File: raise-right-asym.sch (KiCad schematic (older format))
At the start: 102 parts, among them IC1 ATTINY88-A, J1 USB_C_Receptacle_16pin, P1 CONN_01X01, P2 CONN_01X01, P3 CONN_01X01, P4 CONN_01X01, P5 CONN_01X01, P6 CONN_01X01, P7 CONN_01X01, P8 CONN_02X03, Q1 Q_PMOS_GSD, SW1 SW_PUSH, SW10 SW_PUSH, SW11 SW_PUSH, SW12 SW_PUSH, SW13 SW_PUSH, SW14 SW_PUSH, SW15 SW_PUSH, SW16 SW_PUSH, SW17 SW_PUSH, SW18 SW_PUSH, SW19 SW_PUSH, SW2 SW_PUSH, SW20 SW_PUSH, SW21 SW_PUSH, SW22 SW_PUSH, SW23 SW_PUSH, SW24 SW_PUSH, SW25 SW_PUSH, SW26 SW_PUSH, SW27 SW_PUSH, SW28 SW_PUSH, SW29 SW_PUSH, SW3 SW_PUSH, SW30 SW_PUSH, SW31 SW_PUSH, SW32 SW_PUSH, SW33 SW_PUSH, SW34 SW_PUSH, SW4 SW_PUSH, SW5 SW_PUSH, SW6 SW_PUSH, SW7 SW_PUSH, SW8 SW_PUSH, SW9 SW_PUSH, U1 ss39et

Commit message: pre align
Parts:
- U1: supplier Value -> Honeywell; supplier PN Value -> SS39ET
- renumbered P5 to T1, P6 to T2, P7 to T3
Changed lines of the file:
@@
 EESchema Schematic File Version 3
 LIBS:raise-right-asym-cache
-LIBS:power
-LIBS:74xx
 EELAYER 26 0
 EELAYER END
@@
 $EndComp
 $Comp
-L CONN_01X01 P5
+L CONN_01X01 T1
 U 1 1 59D8FBB7
 P 5050 5650
-F 0 "P5" H 5128 5691 50  0000 L CNN
+F 0 "T1" H 5128 5691 50  0000 L CNN
 F 1 "CONN_01X01" H 5128 5600 50  0000 L CNN
 F 2 "raise_fp:MountingHole_5.5mm" H 5050 5650 50  0001 C CNN
@@
 D
 $Comp
-L CONN_01X01 P6
+L CONN_01X01 T2
 U 1 1 5A32AD50
 P 5050 5800
-F 0 "P6" H 5128 5841 50  0000 L CNN
+F 0 "T2" H 5128 5841 50  0000 L CNN
 F 1 "CONN_01X01" H 5128 5750 50  0000 L CNN
 F 2 "raise_fp:MountingHole_5.5mm" H 5050 5800 50  0001 C CNN
@@
 $EndComp
 $Comp
-L CONN_01X01 P7
+L CONN_01X01 T3
 U 1 1 5A32AD56
 P 5050 5950
-F 0 "P7" H 5128 5991 50  0000 L CNN
+F 0 "T3" H 5128 5991 50  0000 L CNN
 F 1 "CONN_01X01" H 5128 5900 50  0000 L CNN
 F 2 "raise_fp:MountingHole_5.5mm" H 5050 5950 50  0001 C CNN
@@
 F 3 "http://www.farnell.com/datasheets/2007294.pdf?_ga=2.106159619.1235724654.1525704504-2043240940.1516888894" H 3850 1350 60  0001 C CNN
 F 4 "2292924" H 3850 1000 60  0001 C CNN "farnell #"
-F 5 "Value" H 3850 1000 60  0001 C CNN "supplier"
-F 6 "Value" H 3850 1000 60  0001 C CNN "supplier PN"
+F 5 "Honeywell" H 3850 1000 60  0001 C CNN "supplier"
+F 6 "SS39ET" H 3850 1000 60  0001 C CNN "supplier PN"
 F 7 "Value" H 3850 1000 60  0001 C CNN "MOQ"
 F 8 "Value" H 3850 1000 60  0001 C CNN "leadtime"

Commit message: post align
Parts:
- renumbered SW-ISO-16 to SW_ISO_16, SW-ISO-8 to SW_ISO_8
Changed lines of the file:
@@
 hall
 $Comp
-L SW_PUSH SW-ISO-8
+L SW_PUSH SW_ISO_8
 U 1 1 5AE3302A
 P 5050 1950
-F 0 "SW-ISO-8" H 5050 2205 50  0000 C CNN
+F 0 "SW_ISO_8" H 5050 2205 50  0000 C CNN
 F 1 "SW_PUSH" H 5050 2114 50  0000 C CNN
 F 2 "raise_fp:kailhsocket-cherry" H 5050 1950 50  0001 C CNN
@@
 $EndComp
 $Comp
-L SW_PUSH SW-ISO-16
+L SW_PUSH SW_ISO_16
 U 1 1 5AE3364E
 P 5050 2650
-F 0 "SW-ISO-16" H 5050 2905 50  0000 C CNN
+F 0 "SW_ISO_16" H 5050 2905 50  0000 C CNN
 F 1 "SW_PUSH" H 5050 2814 50  0000 C CNN
 F 2 "raise_fp:kailhsocket-cherry" H 5050 2650 50  0001 C CNN

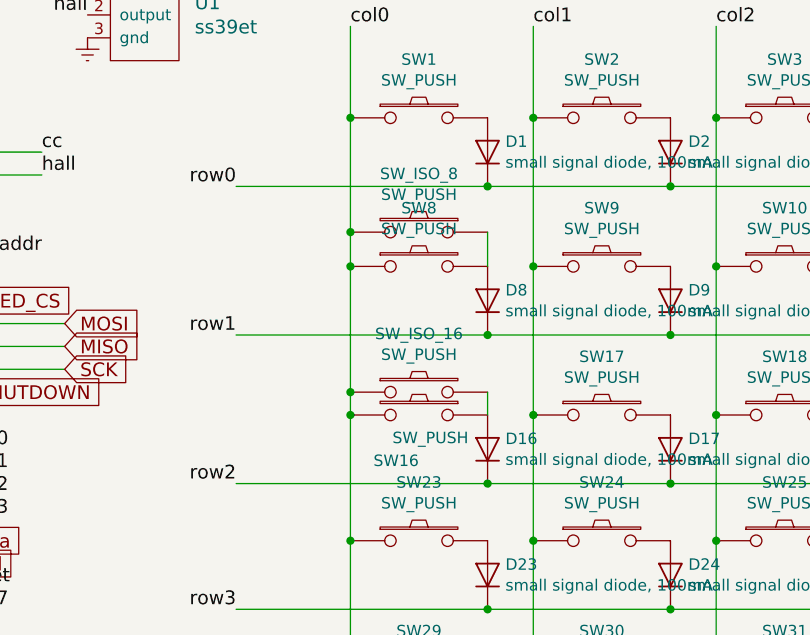
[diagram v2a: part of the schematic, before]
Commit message: fixed diodes
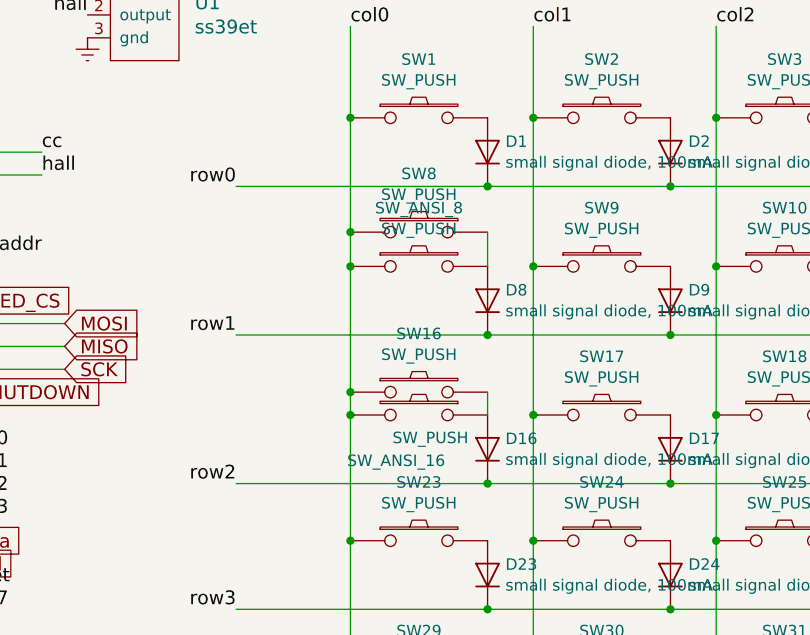
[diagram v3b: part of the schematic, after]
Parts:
- SW_ANSI_16: renamed from SW16; MOQ (none) -> Value; leadtime (none) -> Value
- SW_ANSI_8: renamed from SW8; MOQ (none) -> Value; leadtime (none) -> Value
- renumbered SW_ISO_16 to SW16, SW_ISO_8 to SW8
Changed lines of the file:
@@
 $EndComp
 $Comp
-L SW_PUSH SW8
+L SW_PUSH SW_ANSI_8
 U 1 1 59958E32
 P 5050 2100
-F 0 "SW8" H 5050 2355 50  0000 C CNN
+F 0 "SW_ANSI_8" H 5050 2355 50  0000 C CNN
 F 1 "SW_PUSH" H 5050 2264 50  0000 C CNN
 F 2 "raise_fp:kailhsocket-cherry" H 5050 2100 50  0001 C CNN
 F 3 "" H 5050 2100 50  0000 C CNN
-F 4 "" H 5050 2100 60  0001 C CNN "farnell #"
-F 5 "kailh" H -50 -300 60  0001 C CNN "supplier"
-F 6 "CPG151101S11" H -50 -300 60  0001 C CNN "supplier PN"
+F 4 "kailh" H -50 -300 60  0001 C CNN "supplier"
+F 5 "CPG151101S11" H -50 -300 60  0001 C CNN "supplier PN"
+F 6 "Value" H 5050 2100 60  0001 C CNN "MOQ"
+F 7 "Value" H 5050 2100 60  0001 C CNN "leadtime"
 	1    5050 2100
 	1    0    0    -1
@@
 $EndComp
 $Comp
-L SW_PUSH SW16
+L SW_PUSH SW_ANSI_16
 U 1 1 59958E38
 P 5050 2750
-F 0 "SW16" H 5150 2550 50  0000 C CNN
+F 0 "SW_ANSI_16" H 5150 2550 50  0000 C CNN
 F 1 "SW_PUSH" H 5000 2650 50  0000 C CNN
 F 2 "raise_fp:kailhsocket-cherry" H 5050 2750 50  0001 C CNN
@@
 F 4 "kailh" H -50 -300 60  0001 C CNN "supplier"
 F 5 "CPG151101S11" H -50 -300 60  0001 C CNN "supplier PN"
+F 6 "Value" H 5050 2750 60  0001 C CNN "MOQ"
+F 7 "Value" H 5050 2750 60  0001 C CNN "leadtime"
 	1    5050 2750
 	-1   0    0    -1
@@
 hall
 $Comp
-L SW_PUSH SW_ISO_8
+L SW_PUSH SW8
 U 1 1 5AE3302A
 P 5050 1950
-F 0 "SW_ISO_8" H 5050 2205 50  0000 C CNN
+F 0 "SW8" H 5050 2205 50  0000 C CNN
 F 1 "SW_PUSH" H 5050 2114 50  0000 C CNN
 F 2 "raise_fp:kailhsocket-cherry" H 5050 1950 50  0001 C CNN
@@
 $EndComp
 $Comp
-L SW_PUSH SW_ISO_16
+L SW_PUSH SW16
 U 1 1 5AE3364E
 P 5050 2650
-F 0 "SW_ISO_16" H 5050 2905 50  0000 C CNN
+F 0 "SW16" H 5050 2905 50  0000 C CNN
 F 1 "SW_PUSH" H 5050 2814 50  0000 C CNN
 F 2 "raise_fp:kailhsocket-cherry" H 5050 2650 50  0001 C CNN

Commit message: new alignment
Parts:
- added F1, F2: CONN_01X01, raise_fp:Fiducial_0.5mm_Dia_1mm_Outer, symbol CONN_01X01
- added R6: 10k, 125mW, 5%, raise_fp:R_0603, symbol R
- SW15, SW22, SW28, SW34, SW7: footprint raise_fp:kailhsocket-cherry -> raise_fp:kailhsocket-cherry-right-joint
- T1, T2, T3: footprint raise_fp:MountingHole_5.5mm -> raise_fp:MountingHole_4.3mm
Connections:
- net labels added: ansi, post_ferrite
- wire segments 43 -> 42
- no-connect marks 9 -> 10
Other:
- moved on the sheet: D34, R1, SW34
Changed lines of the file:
@@
 F 0 "SW28" H 9050 3555 50  0000 C CNN
 F 1 "SW_PUSH" H 9050 3464 50  0000 C CNN
-F 2 "raise_fp:kailhsocket-cherry" H 9050 3300 50  0001 C CNN
+F 2 "raise_fp:kailhsocket-cherry-right-joint" H 9050 3300 50  0001 C CNN
 F 3 "" H 9050 3300 50  0000 C CNN
 F 4 "kailh" H -50 -300 60  0001 C CNN "supplier"
@@
 F 0 "SW7" H 9850 1705 50  0000 C CNN
 F 1 "SW_PUSH" H 9850 1614 50  0000 C CNN
-F 2 "raise_fp:kailhsocket-cherry" H 9850 1450 50  0001 C CNN
+F 2 "raise_fp:kailhsocket-cherry-right-joint" H 9850 1450 50  0001 C CNN
 F 3 "" H 9850 1450 50  0000 C CNN
 F 4 "kailh" H -50 -300 60  0001 C CNN "supplier"
@@
 scl
 NoConn ~ 3050 1900
-Text Notes 8600 3850 0    60   ~ 0
+Text Notes 9600 3950 0    60   ~ 0
 2 extra switches are on another PCB
-Text GLabel 1900 5000 2    60   Input ~ 0
-SHUTDOWN
 $Comp
 L R R1
 U 1 1 59D3AEF6
-P 1900 5150
-F 0 "R1" H 1970 5196 50  0000 L CNN
-F 1 "10k, 125mW, 5%" V 1700 4800 50  0000 L CNN
-F 2 "raise_fp:R_0603" V 1830 5150 50  0001 C CNN
-F 3 "" H 1900 5150 50  0000 C CNN
-F 4 "2447230" H 1900 5150 60  0001 C CNN "farnell #"
-F 5 "any/open" H -3700 -100 60  0001 C CNN "supplier"
-	1    1900 5150
-	1    0    0    -1
-$EndComp
-$Comp
-L Earth #PWR013
-U 1 1 59D3B0CC
-P 1900 5300
-F 0 "#PWR013" H 1900 5050 50  0001 C CNN
-F 1 "Earth" H 1900 5150 50  0001 C CNN
-F 2 "" H 1900 5300 50  0000 C CNN
-F 3 "" H 1900 5300 50  0000 C CNN
-	1    1900 5300
+P 1900 5200
+F 0 "R1" H 1970 5246 50  0000 L CNN
+F 1 "10k, 125mW, 5%" V 1700 4850 50  0000 L CNN
+F 2 "raise_fp:R_0603" V 1830 5200 50  0001 C CNN
+F 3 "" H 1900 5200 50  0000 C CNN
+F 4 "2447230" H 1900 5200 60  0001 C CNN "farnell #"
+F 5 "any/open" H -3700 -50 60  0001 C CNN "supplier"
+	1    1900 5200
 	1    0    0    -1
 $EndComp
@@
 F 0 "SW22" H 9850 3005 50  0000 C CNN
 F 1 "SW_PUSH" H 9850 2914 50  0000 C CNN
-F 2 "raise_fp:kailhsocket-cherry" H 9850 2750 50  0001 C CNN
+F 2 "raise_fp:kailhsocket-cherry-right-joint" H 9850 2750 50  0001 C CNN
 F 3 "" H 9850 2750 50  0000 C CNN
 F 4 "kailh" H -50 -300 60  0001 C CNN "supplier"
@@
 F 0 "SW15" H 10650 2355 50  0000 C CNN
 F 1 "SW_PUSH" H 10650 2264 50  0000 C CNN
-F 2 "raise_fp:kailhsocket-cherry" H 10650 2100 50  0001 C CNN
+F 2 "raise_fp:kailhsocket-cherry-right-joint" H 10650 2100 50  0001 C CNN
 F 3 "" H 10650 2100 50  0000 C CNN
 F 4 "kailh" H -50 -300 60  0001 C CNN "supplier"
@@
 L SW_PUSH SW34
 U 1 1 59D7CCDF
-P 10650 3950
-F 0 "SW34" H 10650 4205 50  0000 C CNN
-F 1 "SW_PUSH" H 10650 4114 50  0000 C CNN
-F 2 "raise_fp:kailhsocket-cherry" H 10650 3950 50  0001 C CNN
-F 3 "" H 10650 3950 50  0000 C CNN
-F 4 "kailh" H -50 -300 60  0001 C CNN "supplier"
-F 5 "CPG151101S11" H -50 -300 60  0001 C CNN "supplier PN"
-	1    10650 3950
+P 9050 3950
+F 0 "SW34" H 9050 4205 50  0000 C CNN
+F 1 "SW_PUSH" H 9050 4114 50  0000 C CNN
+F 2 "raise_fp:kailhsocket-cherry-right-joint" H 9050 3950 50  0001 C CNN
+F 3 "" H 9050 3950 50  0000 C CNN
+F 4 "kailh" H -1650 -300 60  0001 C CNN "supplier"
+F 5 "CPG151101S11" H -1650 -300 60  0001 C CNN "supplier PN"
+	1    9050 3950
 	1    0    0    -1
 $EndComp
@@
 L D D34
 U 1 1 59D7CCE5
-P 10950 4100
-F 0 "D34" V 10996 4022 50  0000 R CNN
-F 1 "small signal diode, 100mA" V 10905 4022 50  0000 R CNN
-F 2 "raise_fp:D_SOD-123" H 10950 4100 50  0001 C CNN
-F 3 "" H 10950 4100 50  0000 C CNN
-F 4 "2454043" H 10950 4100 60  0001 C CNN "farnell #"
-F 5 "any/open" H -50 -300 60  0001 C CNN "supplier"
-	1    10950 4100
+P 9350 4100
+F 0 "D34" V 9396 4022 50  0000 R CNN
+F 1 "small signal diode, 100mA" V 9305 4022 50  0000 R CNN
+F 2 "raise_fp:D_SOD-123" H 9350 4100 50  0001 C CNN
+F 3 "" H 9350 4100 50  0000 C CNN
+F 4 "2454043" H 9350 4100 60  0001 C CNN "farnell #"
+F 5 "any/open" H -1650 -300 60  0001 C CNN "supplier"
+	1    9350 4100
 	0    -1   -1   0
 $EndComp
@@
 F 0 "T1" H 5128 5691 50  0000 L CNN
 F 1 "CONN_01X01" H 5128 5600 50  0000 L CNN
-F 2 "raise_fp:MountingHole_5.5mm" H 5050 5650 50  0001 C CNN
+F 2 "raise_fp:MountingHole_4.3mm" H 5050 5650 50  0001 C CNN
 F 3 "" H 5050 5650 50  0000 C CNN
 F 4 "dnp" H 5050 5650 60  0001 C CNN "farnell #"
@@
 F 0 "T2" H 5128 5841 50  0000 L CNN
 F 1 "CONN_01X01" H 5128 5750 50  0000 L CNN
-F 2 "raise_fp:MountingHole_5.5mm" H 5050 5800 50  0001 C CNN
+F 2 "raise_fp:MountingHole_4.3mm" H 5050 5800 50  0001 C CNN
 F 3 "" H 5050 5800 50  0000 C CNN
 F 4 "dnp" H 5050 5800 60  0001 C CNN "farnell #"
@@
 F 0 "T3" H 5128 5991 50  0000 L CNN
 F 1 "CONN_01X01" H 5128 5900 50  0000 L CNN
-F 2 "raise_fp:MountingHole_5.5mm" H 5050 5950 50  0001 C CNN
+F 2 "raise_fp:MountingHole_4.3mm" H 5050 5950 50  0001 C CNN
 F 3 "" H 5050 5950 50  0000 C CNN
 F 4 "dnp" H 5050 5950 60  0001 C CNN "farnell #"
@@
 	0    1    1    0
 $EndComp
-NoConn ~ 3050 2150
 Text Label 3400 1600 0    60   ~ 0
 cc
@@
 P 7100 4750
 F 0 "L1" V 7100 4950 50  0000 C CNN
-F 1 "Ferrite_Bead_Small" V 7250 5000 50  0000 C CNN
+F 1 "Ferrite_Bead_Small" V 7100 5400 50  0000 C CNN
 F 2 "raise_fp:R_0603" V 7030 4750 50  0001 C CNN
 F 3 "" H 7100 4750 50  0001 C CNN
@@
 Connection ~ 4750 2750
 Wire Wire Line
-	4250 4250 10950 4250
+	4250 4250 9350 4250
 Wire Wire Line
 	4250 3600 9350 3600
@@
 Connection ~ 9350 2400
 Wire Wire Line
-	8750 1050 8750 3300
+	8750 1050 8750 3950
 Connection ~ 8750 1450
 Connection ~ 9350 3050
@@
 Wire Wire Line
 	4000 6600 4000 6700
-Wire Wire Line
-	10350 1050 10350 3950
-Connection ~ 10350 2100
 Connection ~ 10150 2400
 Connection ~ 9550 2750
 Connection ~ 9550 2100
-Connection ~ 10350 1450
 Wire Wire Line
 	900  5500 900  5350
@@
 	6900 5700 6900 5800
 Wire Wire Line
-	6900 4900 6900 4700
+	6900 4700 6900 4900
 Wire Wire Line
 	6900 4750 7000 4750
@@
 Wire Wire Line
 	2500 7350 2800 7350
-Connection ~ 10350 1950
-Wire Wire Line
-	10950 1950 10950 2100
 Connection ~ 4750 2650
 Wire Wire Line
@@
 Text Label 10400 5950 2    60   ~ 0
 row7
-Text Label 10400 5850 2    60   ~ 0
+Text Label 10400 5750 2    60   ~ 0
 col6
-Text Label 10400 5750 2    60   ~ 0
-col5
 $Comp
 L TEST TP8
@@
 Text Label 7350 5250 0    60   ~ 0
 cc
+Text Label 6900 4900 0    60   ~ 0
+post_ferrite
+Connection ~ 9350 4250
+Wire Wire Line
+	10350 2100 10350 1050
+Text Label 10400 5850 2    60   ~ 0
+col7
+$Comp
+L CONN_01X01 F1
+U 1 1 5B23BDC0
+P 5050 6150
+F 0 "F1" H 5128 6191 50  0000 L CNN
+F 1 "CONN_01X01" H 5128 6100 50  0000 L CNN
+F 2 "raise_fp:Fiducial_0.5mm_Dia_1mm_Outer" H 5050 6150 50  0001 C CNN
+F 3 "" H 5050 6150 50  0000 C CNN
+F 4 "dnp" H 5050 6150 60  0001 C CNN "farnell #"
+F 5 "dnp" H 3900 200 60  0001 C CNN "supplier"
+F 6 "Value" H 5050 6150 60  0001 C CNN "supplier PN"
+F 7 "Value" H 5050 6150 60  0001 C CNN "MOQ"
+F 8 "Value" H 5050 6150 60  0001 C CNN "leadtime"
+	1    5050 6150
+	1    0    0    -1
+$EndComp
+$Comp
+L CONN_01X01 F2
+U 1 1 5B23BDCB
+P 5050 6300
+F 0 "F2" H 5128 6341 50  0000 L CNN
+F 1 "CONN_01X01" H 5128 6250 50  0000 L CNN
+F 2 "raise_fp:Fiducial_0.5mm_Dia_1mm_Outer" H 5050 6300 50  0001 C CNN
+F 3 "" H 5050 6300 50  0000 C CNN
+F 4 "dnp" H 5050 6300 60  0001 C CNN "farnell #"
+F 5 "dnp" H 3900 200 60  0001 C CNN "supplier"
+F 6 "Value" H 5050 6300 60  0001 C CNN "supplier PN"
+F 7 "Value" H 5050 6300 60  0001 C CNN "MOQ"
+F 8 "Value" H 5050 6300 60  0001 C CNN "leadtime"
+	1    5050 6300
+	1    0    0    -1
+$EndComp
+NoConn ~ 4850 6150
+NoConn ~ 4850 6300
+Text Label 3050 2150 0    60   ~ 0
+ansi
+Text GLabel 2350 5000 2    60   Input ~ 0
+SHUTDOWN
+$Comp
+L R R6
+U 1 1 5B277E2E
+P 2350 5150
+F 0 "R6" H 2420 5196 50  0000 L CNN
+F 1 "10k, 125mW, 5%" V 2150 4800 50  0000 L CNN
+F 2 "raise_fp:R_0603" V 2280 5150 50  0001 C CNN
+F 3 "" H 2350 5150 50  0000 C CNN
+F 4 "2447230" H 2350 5150 60  0001 C CNN "farnell #"
+F 5 "any/open" H -3250 -100 60  0001 C CNN "supplier"
+	1    2350 5150
+	1    0    0    -1
+$EndComp
+$Comp
+L Earth #PWR013
+U 1 1 5B277E34
+P 2350 5300
+F 0 "#PWR013" H 2350 5050 50  0001 C CNN
+F 1 "Earth" H 2350 5150 50  0001 C CNN
+F 2 "" H 2350 5300 50  0000 C CNN
+F 3 "" H 2350 5300 50  0000 C CNN
+	1    2350 5300
+	1    0    0    -1
+$EndComp
+$Comp
+L +5V #PWR036
+U 1 1 5B277F75
+P 1900 5050
+F 0 "#PWR036" H 1900 4900 50  0001 C CNN
+F 1 "+5V" H 1915 5223 50  0000 C CNN
+F 2 "" H 1900 5050 50  0000 C CNN
+F 3 "" H 1900 5050 50  0000 C CNN
+	1    1900 5050
+	1    0    0    -1
+$EndComp
+Text Label 1900 5350 3    60   ~ 0
+ansi
 $EndSCHEMATC

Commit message: pre routing
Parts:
- added R7: 0R, raise_fp:R_0603, symbol R
- P8: footprint raise_fp:Tag-Connect_TC2030-IDC-NL -> raise_fp:icsp-2.54-smt
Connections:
- wire segments 42 -> 45
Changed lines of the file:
@@
 F 0 "P8" H 1150 7650 50  0000 C CNN
 F 1 "CONN_02X03" H 1150 7250 50  0000 C CNN
-F 2 "raise_fp:Tag-Connect_TC2030-IDC-NL" H 1150 6250 60  0001 C CNN
+F 2 "raise_fp:icsp-2.54-smt" H 1150 6250 60  0001 C CNN
 F 3 "" H 1150 6250 60  0000 C CNN
 F 4 "dnp" H 1150 7450 60  0001 C CNN "farnell #"
@@
 	3100 6900 3100 7000
 Wire Wire Line
-	2800 6600 2800 6650
+	2800 6300 2800 6650
 Connection ~ 2800 6600
 Wire Wire Line
@@
 Text Label 1900 5350 3    60   ~ 0
 ansi
+$Comp
+L R R7
+U 1 1 5B2B6980
+P 3100 6300
+F 0 "R7" H 3170 6346 50  0000 L CNN
+F 1 "0R" H 3170 6255 50  0000 L CNN
+F 2 "raise_fp:R_0603" V 3030 6300 50  0001 C CNN
+F 3 "" H 3100 6300 50  0000 C CNN
+F 4 "dnp" H 3100 6300 60  0001 C CNN "farnell #"
+F 5 "dnp" H 300 -900 60  0001 C CNN "supplier"
+F 6 "Value" H 3100 6300 60  0001 C CNN "supplier PN"
+F 7 "Value" H 3100 6300 60  0001 C CNN "MOQ"
+F 8 "Value" H 3100 6300 60  0001 C CNN "leadtime"
+	1    3100 6300
+	0    1    1    0
+$EndComp
+Wire Wire Line
+	2950 6300 2800 6300
+Wire Wire Line
+	3250 6300 3550 6300
+Wire Wire Line
+	3550 6300 3550 6600
 $EndSCHEMATC

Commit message: iso/ansi component naming
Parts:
- D_ANSI_ISO_16: renamed from D16; MOQ (none) -> Value; leadtime (none) -> Value; supplier PN (none) -> Value
- D_ANSI_ISO_8: renamed from D8; MOQ (none) -> Value; leadtime (none) -> Value; supplier PN (none) -> Value
- R_ANSI_1: renamed from R1; MOQ (none) -> Value; leadtime (none) -> Value; supplier PN (none) -> Value
- renumbered SW16 to SW_ISO_16, SW8 to SW_ISO_8
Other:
- note added: "firmware pulls addr lines low,\nplace R to make high\nonly place on RHS\n\n"
- note removed: "firmware pulls addr lines low,\nplace R to make high\n"
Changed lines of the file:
@@
 $EndComp
 $Comp
-L D D8
+L D D_ANSI_ISO_8
 U 1 1 59958E34
 P 5350 2250
-F 0 "D8" V 5396 2172 50  0000 R CNN
+F 0 "D_ANSI_ISO_8" V 5396 2172 50  0000 R CNN
 F 1 "small signal diode, 100mA" V 5305 2172 50  0000 R CNN
 F 2 "raise_fp:D_SOD-123" H 5350 2250 50  0001 C CNN
@@
 F 4 "2454043" H 5350 2250 60  0001 C CNN "farnell #"
 F 5 "any/open" H -50 -300 60  0001 C CNN "supplier"
+F 6 "Value" H 5350 2250 60  0001 C CNN "supplier PN"
+F 7 "Value" H 5350 2250 60  0001 C CNN "MOQ"
+F 8 "Value" H 5350 2250 60  0001 C CNN "leadtime"
 	1    5350 2250
 	0    -1   -1   0
@@
 $EndComp
 $Comp
-L D D16
+L D D_ANSI_ISO_16
 U 1 1 59958E39
 P 5350 2900
-F 0 "D16" V 5396 2822 50  0000 R CNN
+F 0 "D_ANSI_ISO_16" V 5396 2822 50  0000 R CNN
 F 1 "small signal diode, 100mA" V 5305 2822 50  0000 R CNN
 F 2 "raise_fp:D_SOD-123" H 5350 2900 50  0001 C CNN
@@
 F 4 "2454043" H 5350 2900 60  0001 C CNN "farnell #"
 F 5 "any/open" H -50 -300 60  0001 C CNN "supplier"
+F 6 "Value" H 5350 2900 60  0001 C CNN "supplier PN"
+F 7 "Value" H 5350 2900 60  0001 C CNN "MOQ"
+F 8 "Value" H 5350 2900 60  0001 C CNN "leadtime"
 	1    5350 2900
 	0    -1   -1   0
@@
 2 extra switches are on another PCB
 $Comp
-L R R1
+L R R_ANSI_1
 U 1 1 59D3AEF6
 P 1900 5200
-F 0 "R1" H 1970 5246 50  0000 L CNN
+F 0 "R_ANSI_1" H 1970 5246 50  0000 L CNN
 F 1 "10k, 125mW, 5%" V 1700 4850 50  0000 L CNN
 F 2 "raise_fp:R_0603" V 1830 5200 50  0001 C CNN
@@
 F 4 "2447230" H 1900 5200 60  0001 C CNN "farnell #"
 F 5 "any/open" H -3700 -50 60  0001 C CNN "supplier"
+F 6 "Value" H 1900 5200 60  0001 C CNN "supplier PN"
+F 7 "Value" H 1900 5200 60  0001 C CNN "MOQ"
+F 8 "Value" H 1900 5200 60  0001 C CNN "leadtime"
 	1    1900 5200
 	1    0    0    -1
@@
 i2c_addr
 Text Notes 700  5850 0    60   ~ 0
-firmware pulls addr lines low,\nplace R to make high\n
+firmware pulls addr lines low,\nplace R to make high\nonly place on RHS\n\n
 $Comp
 L C C4
@@
 hall
 $Comp
-L SW_PUSH SW8
+L SW_PUSH SW_ISO_8
 U 1 1 5AE3302A
 P 5050 1950
-F 0 "SW8" H 5050 2205 50  0000 C CNN
+F 0 "SW_ISO_8" H 5050 2205 50  0000 C CNN
 F 1 "SW_PUSH" H 5050 2114 50  0000 C CNN
 F 2 "raise_fp:kailhsocket-cherry" H 5050 1950 50  0001 C CNN
@@
 $EndComp
 $Comp
-L SW_PUSH SW16
+L SW_PUSH SW_ISO_16
 U 1 1 5AE3364E
 P 5050 2650
-F 0 "SW16" H 5050 2905 50  0000 C CNN
+F 0 "SW_ISO_16" H 5050 2905 50  0000 C CNN
 F 1 "SW_PUSH" H 5050 2814 50  0000 C CNN
 F 2 "raise_fp:kailhsocket-cherry" H 5050 2650 50  0001 C CNN

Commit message: ansi/iso bom
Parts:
- L1: value Ferrite_Bead_Small -> 470R at 100M, 1A; symbol Ferrite_Bead_Small -> Ferrite_Bead; MOQ (none) -> Value; leadtime (none) -> Value; supplier (none) -> Murata; supplier PN (none) -> BLM18PG471SN1D
- Q1: value Q_PMOS_GSD -> PMOS, -3.6A, 0.02R; MOQ (none) -> Value; leadtime (none) -> Value
- R4, R5: value 5.1k, 125mW, 1% -> 5.1k, 125mW, 5%
- SW1, SW10, SW11, SW12, SW13, SW14, SW15, SW17, SW18, SW19, SW2, SW20, SW21, SW22, SW23, SW24, SW25, SW26, SW27, SW28, SW29, SW3, SW30, SW31, SW32, SW33, SW34, SW4, SW5, SW6, SW7, SW9, SW_ANSI_16, SW_ANSI_8, SW_ISO_16, SW_ISO_8: value SW_PUSH -> kailh hot plug sockets
- TP1: MOQ (none) -> Value; leadtime (none) -> Value; supplier (none) -> dnp; supplier PN (none) -> Value
- TP2, TP3, TP4, TP5, TP6, TP7, TP8, TP9: supplier (none) -> dnp
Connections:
- no-connect marks 10 -> 11
